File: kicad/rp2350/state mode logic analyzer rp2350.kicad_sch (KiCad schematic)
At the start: 127 parts, among them J1 USB0, J10 Vcca_select, J2 5V USB0, J3 Probe_Hi, J4 Probe Power, J5 Probe_Lo, J6 Probe Power, J7 SWD0, J8 FTDI Header, J9 Vccb_select, SW1 Reset, SW2 Boot, U1 MCP4725A2T-E/CH, U12 SN74LVC8T245, U13 SN74LVC2T45DCUR, U2 RP2350_Stamp_XL, U4 SN74LVC8T245, U5 SN74LVC8T245, U6 SN74LVC8T245

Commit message: early pcb layout - need to build a demo/test board next
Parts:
- removed J2: 5V USB0, Connector_PinHeader_2.54mm:PinHeader_1x03_P2.54mm_Vertical, symbol Connector_Generic:Conn_01x03
- removed R8, R9: 27, Resistor_SMD:R_0603_1608Metric_Pad0.98x0.95mm_HandSolder, symbol Device:R_Small
- removed TP100, TP101, TP102, TP103, TP104, TP105, TP106, TP107, TP108, TP109, TP110, TP111, TP112, TP113, TP114, TP115, TP116, TP117, TP118, TP119, TP120, TP121, TP122, TP123, TP124, TP125, TP126, TP127, TP128, TP129, TP130, TP131, TP132, TP133: TestPoint_Harwin, My Libraries:Harwin-S1751-46-Test-Point, symbol My Library:TestPoint_Harwin
- added R7: 10k, Resistor_SMD:R_0603_1608Metric, symbol Device:R_Small
- J10: footprint (none) -> Connector_PinHeader_2.54mm:PinHeader_2x01_P2.54mm_Vertical
- R11: value 1k -> 10k; now fitted
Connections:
- net VBUS is gone; now on net +5V: D6.3 (K), J1.A4 (VBUS), J1.A9 (VBUS), J1.B4 (VBUS), J1.B9 (VBUS)
- net DN: now also J1.A7 (D-), J1.B7 (D-)
- net DP: now also J1.A6 (D+), J1.B6 (D+)
- net GND: now also R7.1; no longer R11.1
- net USB_DN: no longer J1.A7 (D-), J1.B7 (D-)
- net USB_DP: no longer J1.A6 (D+), J1.B6 (D+)
- net Vdac: now reaches U2.54 (GPIO43)
- net Vdac: now also R11.1, R7.2
- no-connect marks 13 -> 12
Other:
- note added: "TODO: - Add OLED Header? - More decoupling for the BUS XCVRs - add ESD protection to inputs"
- note added: "if build a test board add a buffer to eval the threshold"
- note removed: "TODO: - Switch to Stamp XL - Add LDO with DigiPot - Add OLED Header? - More decoupling for the BUS XCVRs - add ESD protection to inputs"

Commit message: pcb initial layout
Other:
- note added: "TODO: - Add OLED Header? - More decoupling for the BUS XCVRs - add ESD protection to inputs - add STEMMA QT Connector"
- note removed: "TODO: - Add OLED Header? - More decoupling for the BUS XCVRs - add ESD protection to inputs"
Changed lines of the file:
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@@
 		)
 	)
-	(text "TODO:\n- Add OLED Header?\n- More decoupling for the BUS XCVRs\n- add ESD protection to inputs\n"
+	(text "TODO:\n- Add OLED Header?\n- More decoupling for the BUS XCVRs\n- add ESD protection to inputs\n- add STEMMA QT Connector\n"
 		(exclude_from_sim no)
 		(at 488.95 27.305 0)

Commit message: added stemma, decoupling caps for buffers -- forgot i was going to start making the dac test board
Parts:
- removed SW1: Reset, Button_Switch_SMD:SW_SPST_PTS810, symbol Switch:SW_Push
- removed SW2: Boot, Button_Switch_SMD:SW_SPST_PTS810, symbol Switch:SW_Push
- added C12, C13, C14, C2, C5: 1u, Capacitor_SMD:C_0603_1608Metric_Pad1.08x0.95mm_HandSolder, symbol Device:C_Small
- added J2: JST_SH_BM04B-SRSS-TB, Connector_JST:JST_SH_BM04B-SRSS-TB_1x04-1MP_P1.00mm_Vertical, symbol Connector_Generic:Conn_01x04
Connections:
- net +3V3: no longer C3.1, C4.1, C7.1, C8.1, C9.1
- net GND: now also C12.2, C13.2, C14.2, C2.2, C5.2, J2.1 (Pin_1)
- net Reset: no longer U2.39 (~{RESET})
- net Vcca: now also C12.1, C13.1, C14.1, C2.1, C5.1
- net Vccb: now also C3.1, C4.1, C7.1, C8.1, C9.1
- new net +3.3V: J2.2 (Pin_2)
- new net SCL: J2.4 (Pin_4)
- new net SDA: J2.3 (Pin_3)
- no-connect marks 12 -> 14
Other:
- note added: "Stemma QT"
- note added: "TODO: - Add OLED Header? - More decoupling for the BUS XCVRs - add ESD protection to inputs"
- note added: "XL has buttons already"
- note removed: "TODO: - Add OLED Header? - More decoupling for the BUS XCVRs - add ESD protection to inputs - add STEMMA QT Connector"

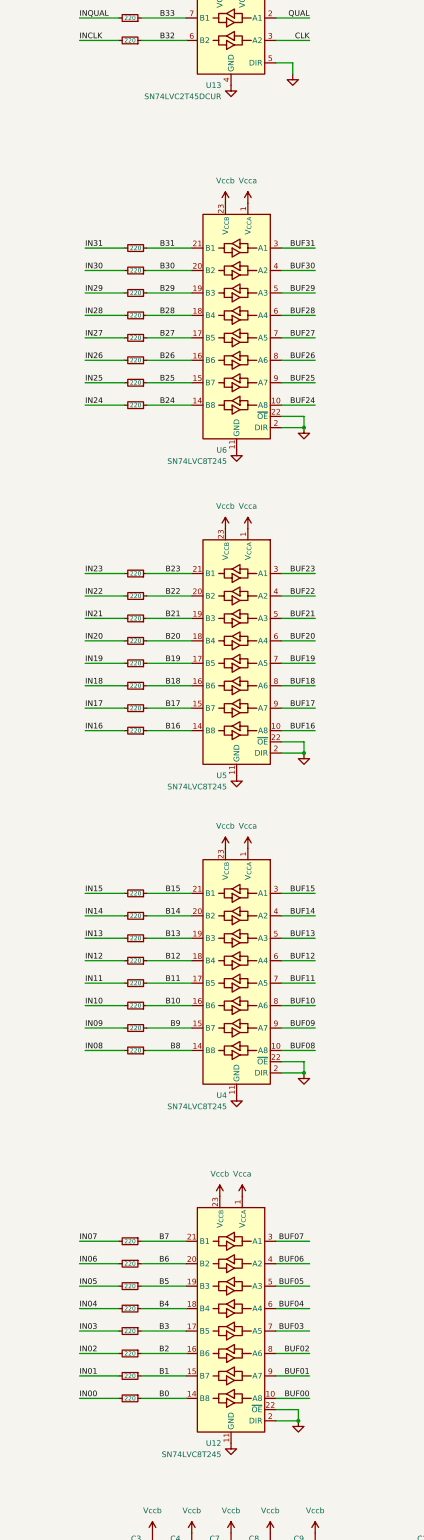
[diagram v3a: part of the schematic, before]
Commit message: updated buffer PNs and reordered pins to match XL pinout
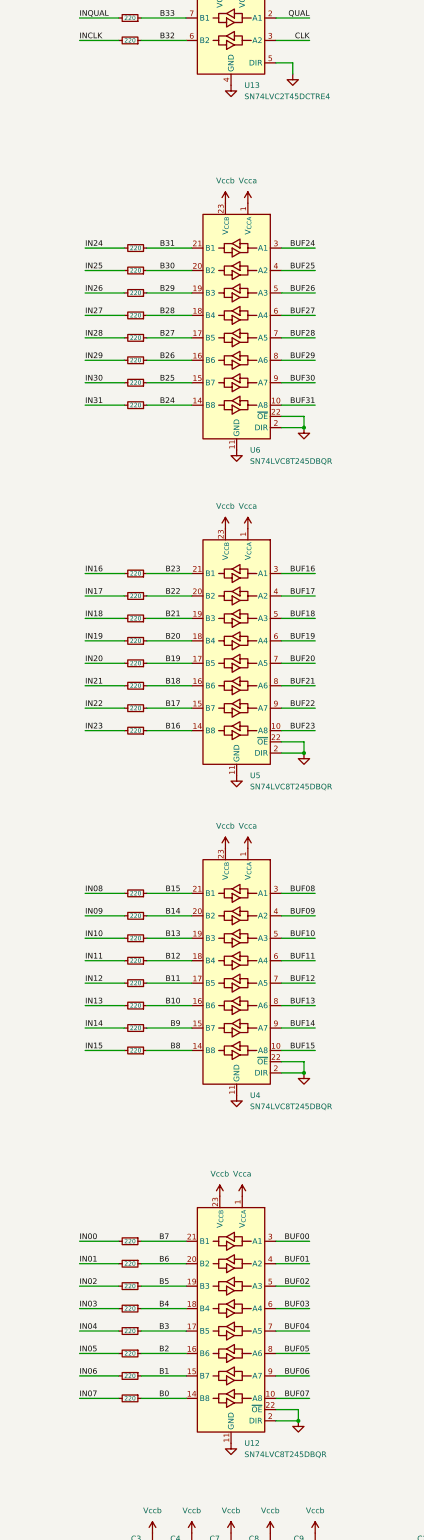
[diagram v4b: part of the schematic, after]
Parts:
- U12, U4, U5, U6: value SN74LVC8T245 -> SN74LVC8T245DBQR
- U13: value SN74LVC2T45DCUR -> SN74LVC2T45DCTRE4; Base PN for SSOP (none) -> SN74LVC2T45DCT
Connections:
- net BUF00: now also U12.3 (A1); no longer U12.10 (A8)
- net BUF01: now also U12.4 (A2); no longer U12.9 (A7)
- net BUF02: now also U12.5 (A3); no longer U12.8 (A6)
- net BUF03: now also U12.6 (A4); no longer U12.7 (A5)
- net BUF04: now also U12.7 (A5); no longer U12.6 (A4)
- net BUF05: now also U12.8 (A6); no longer U12.5 (A3)
- net BUF06: now also U12.9 (A7); no longer U12.4 (A2)
- net BUF07: now also U12.10 (A8); no longer U12.3 (A1)
- net BUF08: now also U4.3 (A1); no longer U4.10 (A8)
- net BUF09: now also U4.4 (A2); no longer U4.9 (A7)
- net BUF10: now also U4.5 (A3); no longer U4.8 (A6)
- net BUF11: now also U4.6 (A4); no longer U4.7 (A5)
- net BUF12: now also U4.7 (A5); no longer U4.6 (A4)
- net BUF13: now also U4.8 (A6); no longer U4.5 (A3)
- net BUF14: now also U4.9 (A7); no longer U4.4 (A2)
- net BUF15: now also U4.10 (A8); no longer U4.3 (A1)
- net BUF16: now also U5.3 (A1); no longer U5.10 (A8)
- net BUF17: now also U5.4 (A2); no longer U5.9 (A7)
- net BUF18: now also U5.5 (A3); no longer U5.8 (A6)
- net BUF19: now also U5.6 (A4); no longer U5.7 (A5)
- net BUF20: now also U5.7 (A5); no longer U5.6 (A4)
- net BUF21: now also U5.8 (A6); no longer U5.5 (A3)
- net BUF22: now also U5.9 (A7); no longer U5.4 (A2)
- net BUF23: now also U5.10 (A8); no longer U5.3 (A1)
- net BUF24: now also U6.3 (A1); no longer U6.10 (A8)
- net BUF25: now also U6.4 (A2); no longer U6.9 (A7)
- net BUF26: now also U6.5 (A3); no longer U6.8 (A6)
- net BUF27: now also U6.6 (A4); no longer U6.7 (A5)
- net BUF28: now also U6.7 (A5); no longer U6.6 (A4)
- net BUF29: now also U6.8 (A6); no longer U6.5 (A3)
- net BUF30: now also U6.9 (A7); no longer U6.4 (A2)
- net BUF31: now also U6.10 (A8); no longer U6.3 (A1)
- net IN00: now also R32.2; no longer R25.2
- net IN01: now also R31.2; no longer R26.2
- net IN02: now also R30.2; no longer R27.2
- net IN03: now also R29.2; no longer R28.2
- net IN04: now also R28.2; no longer R29.2
- net IN05: now also R27.2; no longer R30.2
- net IN06: now also R26.2; no longer R31.2
- net IN07: now also R25.2; no longer R32.2
- net IN08: now also R33.2; no longer R40.2
- net IN09: now also R34.2; no longer R39.2
- net IN10: now also R35.2; no longer R38.2
- net IN11: now also R36.2; no longer R37.2
- net IN12: now also R37.2; no longer R36.2
- net IN13: now also R38.2; no longer R35.2
- net IN14: now also R39.2; no longer R34.2
- net IN15: now also R40.2; no longer R33.2
- net IN16: now also R49.2; no longer R56.2
- net IN17: now also R50.2; no longer R55.2
- net IN18: now also R51.2; no longer R54.2
- net IN19: now also R52.2; no longer R53.2
- net IN20: now also R53.2; no longer R52.2
- net IN21: now also R54.2; no longer R51.2
- net IN22: now also R55.2; no longer R50.2
- net IN23: now also R56.2; no longer R49.2
- net IN24: now also R57.2; no longer R64.2
- net IN25: now also R58.2; no longer R63.2
- net IN26: now also R59.2; no longer R62.2
- net IN27: now also R60.2; no longer R61.2
- net IN28: now also R61.2; no longer R60.2
- net IN29: now also R62.2; no longer R59.2
- net IN30: now also R63.2; no longer R58.2
- net IN31: now also R64.2; no longer R57.2

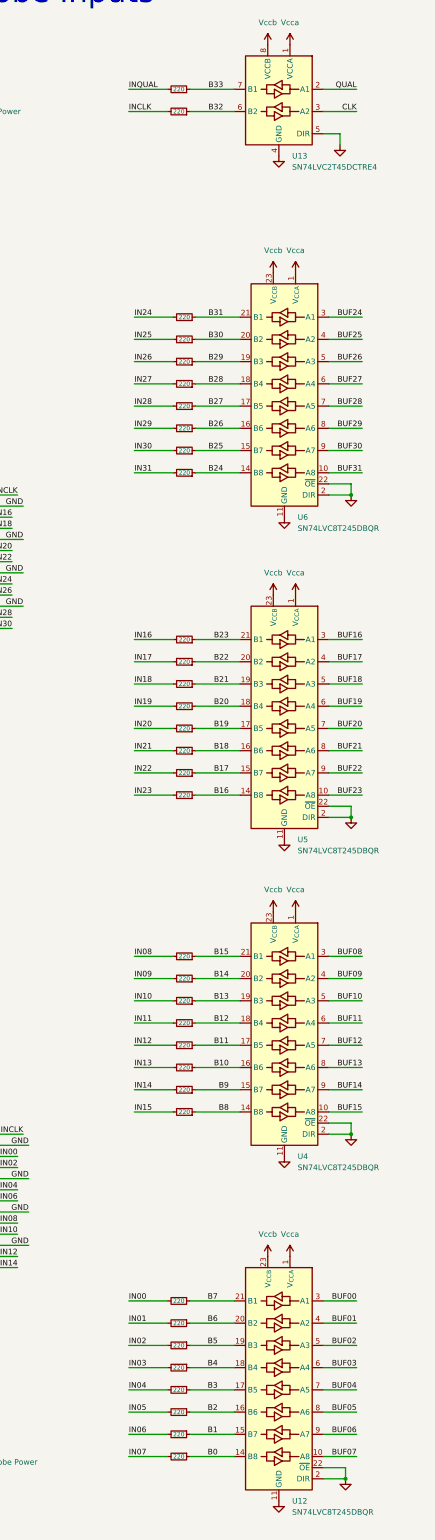
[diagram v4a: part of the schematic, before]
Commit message: replaces term resistors with arrays
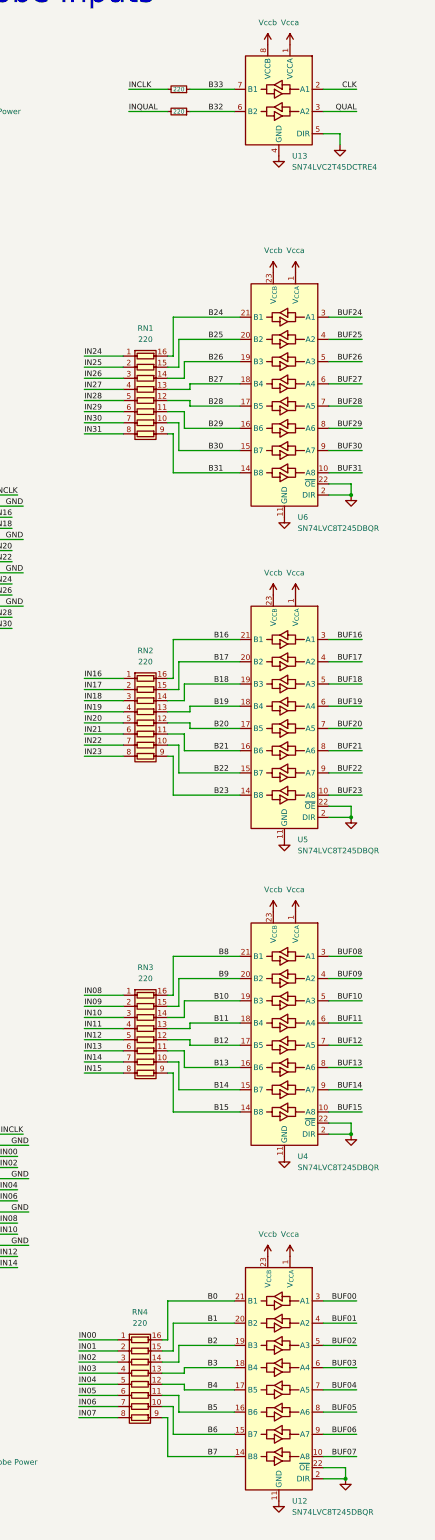
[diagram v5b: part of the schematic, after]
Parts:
- removed R25, R26, R27, R28, R29, R30, R31, R32, R33, R34, R35, R36, R37, R38, R39, R40, R49, R50, R51, R52, R53, R54, R55, R56, R57, R58, R59, R60, R61, R62, R63, R64: 220, Resistor_SMD:R_0603_1608Metric, symbol Device:R_Small
- added RN1, RN2, RN3, RN4: YC248-FR-07220RL, Resistor_SMD:R_Array_Convex_8x0602, symbol Device:R_Pack08
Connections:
- net B0: now also U12.21 (B1), RN4.16 (R1.2); no longer U12.14 (B8)
- net B1: now also U12.20 (B2), RN4.15 (R2.2); no longer U12.15 (B7)
- net B10: now also U4.19 (B3), RN3.14 (R3.2); no longer U4.16 (B6)
- net B11: now also U4.18 (B4), RN3.13 (R4.2); no longer U4.17 (B5)
- net B12: now also U4.17 (B5), RN3.12 (R5.2); no longer U4.18 (B4)
- net B13: now also U4.16 (B6), RN3.11 (R6.2); no longer U4.19 (B3)
- net B14: now also U4.15 (B7), RN3.10 (R7.2); no longer U4.20 (B2)
- net B15: now also U4.14 (B8), RN3.9 (R8.2); no longer U4.21 (B1)
- net B16: now also U5.21 (B1), RN2.16 (R1.2); no longer U5.14 (B8)
- net B17: now also U5.20 (B2), RN2.15 (R2.2); no longer U5.15 (B7)
- net B18: now also U5.19 (B3), RN2.14 (R3.2); no longer U5.16 (B6)
- net B19: now also U5.18 (B4), RN2.13 (R4.2); no longer U5.17 (B5)
- net B2: now also U12.19 (B3), RN4.14 (R3.2); no longer U12.16 (B6)
- net B20: now also U5.17 (B5), RN2.12 (R5.2); no longer U5.18 (B4)
- net B21: now also U5.16 (B6), RN2.11 (R6.2); no longer U5.19 (B3)
- net B22: now also U5.15 (B7), RN2.10 (R7.2); no longer U5.20 (B2)
- net B23: now also U5.14 (B8), RN2.9 (R8.2); no longer U5.21 (B1)
- net B24: now also U6.21 (B1), RN1.16 (R1.2); no longer U6.14 (B8)
- net B25: now also U6.20 (B2), RN1.15 (R2.2); no longer U6.15 (B7)
- net B26: now also U6.19 (B3), RN1.14 (R3.2); no longer U6.16 (B6)
- net B27: now also U6.18 (B4), RN1.13 (R4.2); no longer U6.17 (B5)
- net B28: now also U6.17 (B5), RN1.12 (R5.2); no longer U6.18 (B4)
- net B29: now also U6.16 (B6), RN1.11 (R6.2); no longer U6.19 (B3)
- net B3: now also U12.18 (B4), RN4.13 (R4.2); no longer U12.17 (B5)
- net B30: now also U6.15 (B7), RN1.10 (R7.2); no longer U6.20 (B2)
- net B31: now also U6.14 (B8), RN1.9 (R8.2); no longer U6.21 (B1)
- net B4: now also U12.17 (B5), RN4.12 (R5.2); no longer U12.18 (B4)
- net B5: now also U12.16 (B6), RN4.11 (R6.2); no longer U12.19 (B3)
- net B6: now also U12.15 (B7), RN4.10 (R7.2); no longer U12.20 (B2)
- net B7: now also U12.14 (B8), RN4.9 (R8.2); no longer U12.21 (B1)
- net B8: now also U4.21 (B1), RN3.16 (R1.2); no longer U4.14 (B8)
- net B9: now also U4.20 (B2), RN3.15 (R2.2); no longer U4.15 (B7)
- net CLK: now also U13.2 (A1); no longer U13.3 (A2)
- net IN00: now also RN4.1 (R1.1)
- net IN01: now also RN4.2 (R2.1)
- net IN02: now also RN4.3 (R3.1)
- net IN03: now also RN4.4 (R4.1)
- net IN04: now also RN4.5 (R5.1)
- net IN05: now also RN4.6 (R6.1)
- net IN06: now also RN4.7 (R7.1)
- net IN07: now also RN4.8 (R8.1)
- net IN08: now also RN3.1 (R1.1)
- net IN09: now also RN3.2 (R2.1)
- net IN10: now also RN3.3 (R3.1)
- net IN11: now also RN3.4 (R4.1)
- net IN12: now also RN3.5 (R5.1)
- net IN13: now also RN3.6 (R6.1)
- net IN14: now also RN3.7 (R7.1)
- net IN15: now also RN3.8 (R8.1)
- net IN16: now also RN2.1 (R1.1)
- net IN17: now also RN2.2 (R2.1)
- net IN18: now also RN2.3 (R3.1)
- net IN19: now also RN2.4 (R4.1)
- net IN20: now also RN2.5 (R5.1)
- net IN21: now also RN2.6 (R6.1)
- net IN22: now also RN2.7 (R7.1)
- net IN23: now also RN2.8 (R8.1)
- net IN24: now also RN1.1 (R1.1)
- net IN25: now also RN1.2 (R2.1)
- net IN26: now also RN1.3 (R3.1)
- net IN27: now also RN1.4 (R4.1)
- net IN28: now also RN1.5 (R5.1)
- net IN29: now also RN1.6 (R6.1)
- net IN30: now also RN1.7 (R7.1)
- net IN31: now also RN1.8 (R8.1)
- net INCLK: now also R73.2; no longer R74.2
- net INQUAL: now also R74.2; no longer R73.2
- net QUAL: now also U13.3 (A2); no longer U13.2 (A1)
